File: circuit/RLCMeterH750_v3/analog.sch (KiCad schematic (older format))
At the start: 100 parts, among them J4 DUT, U10 AD8031, U11 AD8031, U12 AD9833, U13 AD8221, U14 AD8221, U16 AD8031, U17 AD8031, U19 FSA3357L8X, U20 FSA3357L8X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

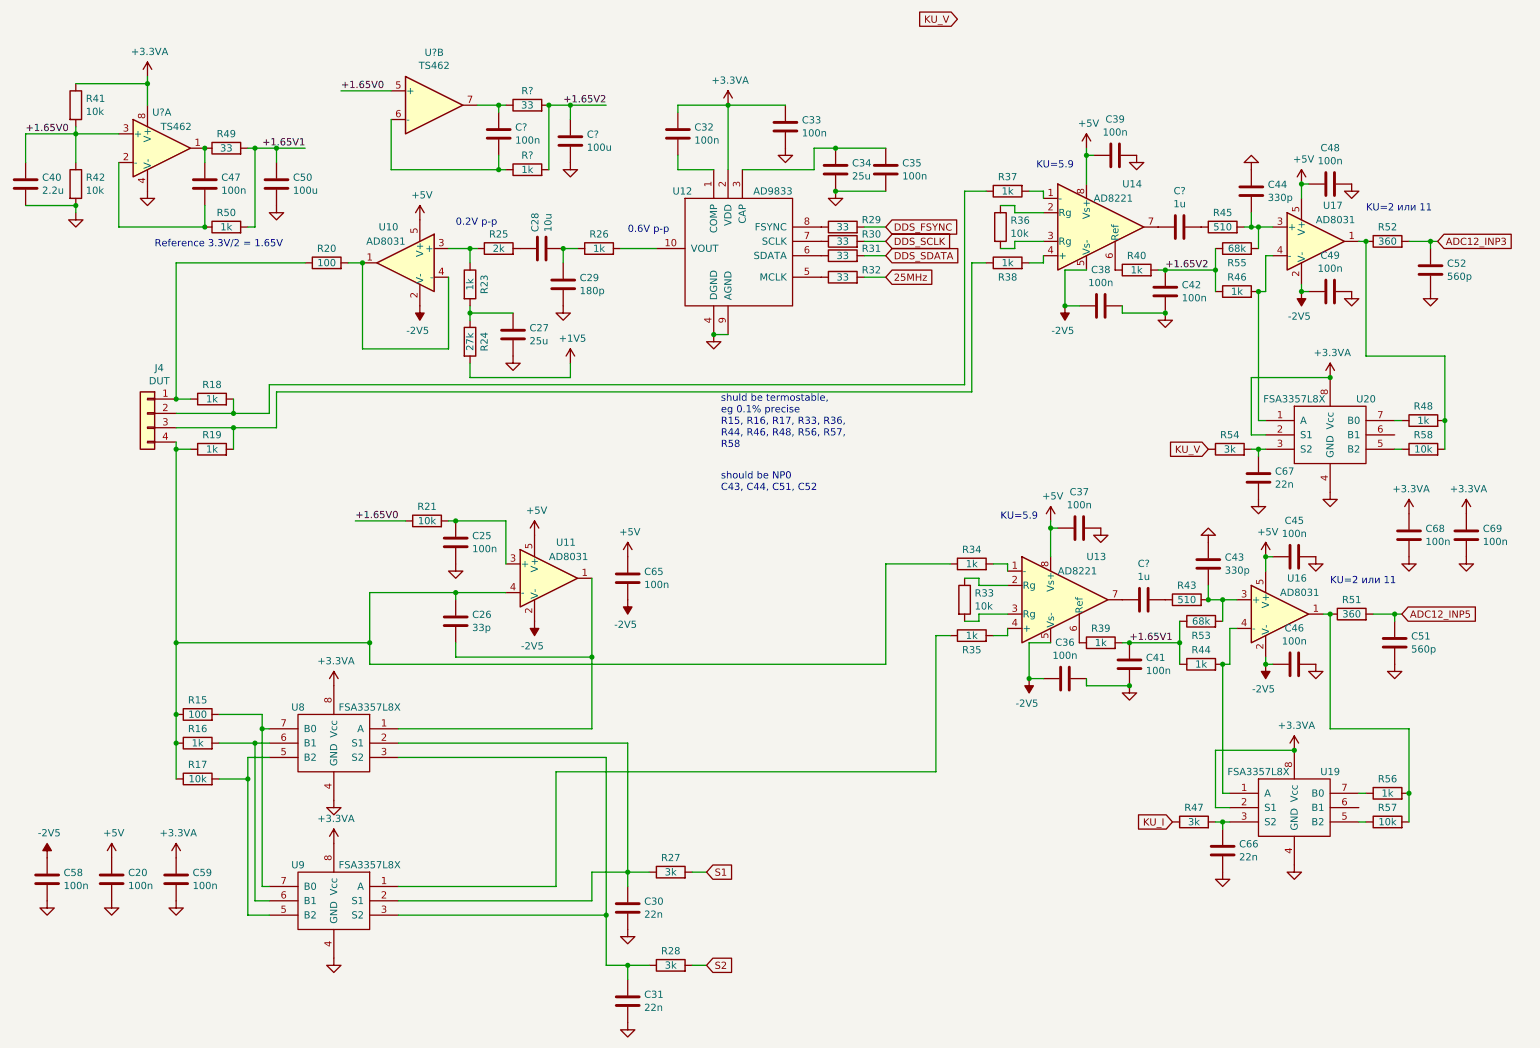
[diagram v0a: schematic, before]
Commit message: - gain_V gain_I надо было умножать, а не делить.
Раньше не проявлялось, так как коэффициэнты были одинаковыми.
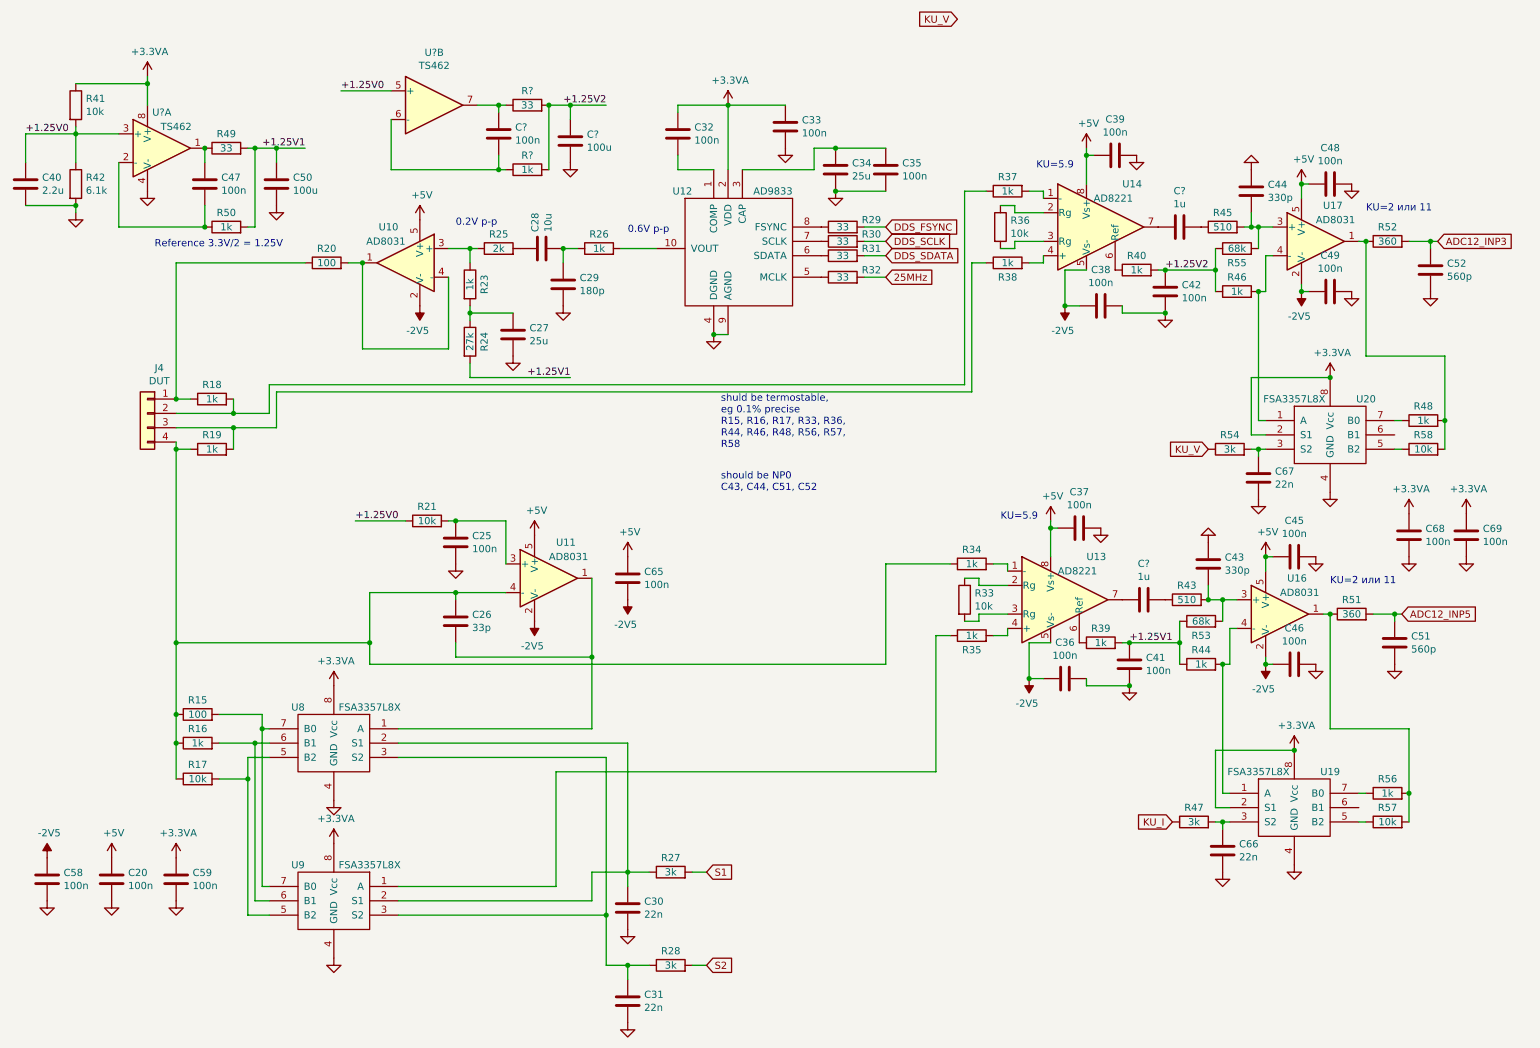
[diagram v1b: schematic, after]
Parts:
- R42: value 10k -> 6.1k
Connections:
- net +1V5 is gone; now on net +1.25V1: R24.2
- net +1.65V0 renamed +1.25V0
- net +1.65V1 renamed +1.25V1
- net +1.65V2 renamed +1.25V2
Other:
- note added: "Reference 3.3V/2 = 1.25V"
- note removed: "Reference 3.3V/2 = 1.65V"
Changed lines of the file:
@@
 Connection ~ 2300 1250
 Text Notes 1600 1950 0    50   ~ 0
-Reference 3.3V/2 = 1.65V
+Reference 3.3V/2 = 1.25V
 $Comp
 L Device:R R42
@@
 P 1050 1500
 F 0 "R42" H 1120 1546 50  0000 L CNN
-F 1 "10k" H 1120 1455 50  0000 L CNN
+F 1 "6.1k" H 1120 1455 50  0000 L CNN
 F 2 "Resistor_SMD:R_0603_1608Metric" V 980 1500 50  0001 C CNN
 F 3 "~" H 1050 1500 50  0001 C CNN
@@
 	1    0    0    -1
 $EndComp
-$Comp
-L power:+1V5 #PWR0181
-U 1 1 5DBA7330
-P 4500 2750
-F 0 "#PWR0181" H 4500 2600 50  0001 C CNN
-F 1 "+1V5" H 4515 2923 50  0000 C CNN
-F 2 "" H 4500 2750 50  0001 C CNN
-F 3 "" H 4500 2750 50  0001 C CNN
-	1    4500 2750
-	1    0    0    -1
-$EndComp
 Wire Wire Line
 	3800 2750 3800 2850
 Wire Wire Line
 	3800 2850 4500 2850
-Wire Wire Line
-	4500 2850 4500 2750
 $Comp
 L Amplifier_Operational:MCP6001-OT U11
@@
 $EndComp
 Text Label 700  1150 0    50   ~ 0
-+1.65V0
++1.25V0
 Wire Wire Line
 	3000 3850 3350 3850
-Text Label 3000 3850 0    50   ~ 0
-+1.65V0
 $Comp
 L Amplifier_Operational:NE5532 U?
@@
 	3250 850  2900 850
 Text Label 2900 850  0    50   ~ 0
-+1.65V0
++1.25V0
 Wire Wire Line
 	2300 1250 2450 1250
@@
 Connection ~ 2450 1250
 Text Label 2350 1250 0    50   ~ 0
-+1.65V1
++1.25V1
 Text Label 4450 950  0    50   ~ 0
-+1.65V2
++1.25V2
 Connection ~ 4350 950
 $Comp
@@
 	4500 950  4750 950
 Text Label 8650 2100 0    50   ~ 0
-+1.65V2
++1.25V2
 Text Label 8400 4700 0    50   ~ 0
-+1.65V1
++1.25V1
 $Comp
 L Device:C C?
@@
 Text Notes 5550 3650 0    50   ~ 0
 should be NP0\nC43, C44, C51, C52
+Text Label 3000 3850 0    50   ~ 0
++1.25V0
+Text Label 4200 2850 0    50   ~ 0
++1.25V1
 $EndSCHEMATC

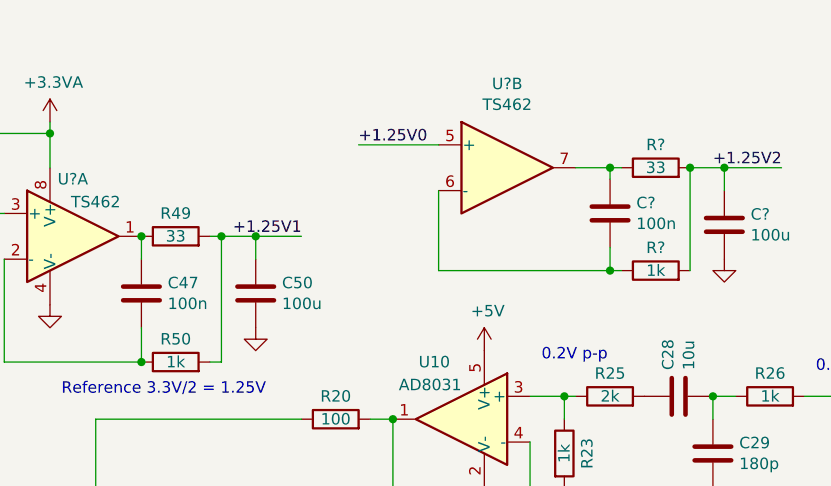
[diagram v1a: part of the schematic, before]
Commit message: - 0 ом резистор на выходе ОУ
- не скалируется график фазы
- стандартные частоты расположены по ряду E12 (экспоненциально)
- добавили коэффииэнты к графикам (KOm, MOm и т.д.)
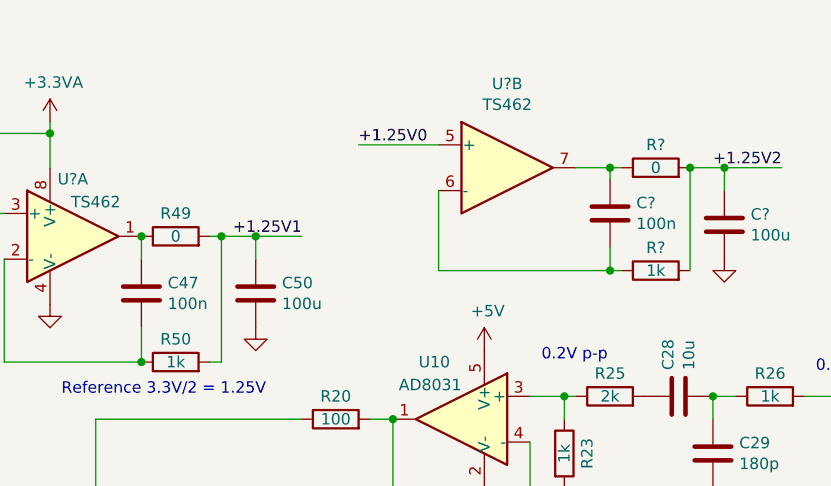
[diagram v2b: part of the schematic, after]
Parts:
- R49, R?: value 33 -> 0
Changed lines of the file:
@@
 P 2100 1250
 F 0 "R49" V 2200 1250 50  0000 C CNN
-F 1 "33" V 2100 1250 50  0000 C CNN
+F 1 "0" V 2100 1250 50  0000 C CNN
 F 2 "Resistor_SMD:R_0603_1608Metric" V 2030 1250 50  0001 C CNN
 F 3 "~" H 2100 1250 50  0001 C CNN
@@
 P 4200 950
 F 0 "R?" V 4300 950 50  0000 C CNN
-F 1 "33" V 4200 950 50  0000 C CNN
+F 1 "0" V 4200 950 50  0000 C CNN
 F 2 "Resistor_SMD:R_0603_1608Metric" V 4130 950 50  0001 C CNN
 F 3 "~" H 4200 950 50  0001 C CNN

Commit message: - все наши страдания с нелинейностью ADC
- debug menu
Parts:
- added C?: 68p, Capacitor_SMD:C_0603_1608Metric, symbol Device:C
- C? (x2): value 1u -> 25u
- R53, R55: value 68k -> 10k
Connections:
- net at C26.1, J4.4 (Pin_4), R15.1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: now also C?.2
- net at R17.2, U8.5 (B2), U9.5 (B2): now also C?.1
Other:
- note added: "Вместо резисторов\nиcпользуем LDO 1.2V"
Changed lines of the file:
@@
 	2400 6600 2250 6600
 Wire Wire Line
-	2250 6600 2250 5650
+	2250 6600 2250 5800
 Wire Wire Line
 	2250 5500 2400 5500
@@
 P 9150 1950
 F 0 "R55" V 9050 1950 50  0000 C CNN
-F 1 "68k" V 9150 1950 50  0000 C CNN
+F 1 "10k" V 9150 1950 50  0000 C CNN
 F 2 "Resistor_SMD:R_0603_1608Metric" V 9080 1950 50  0001 C CNN
 F 3 "~" H 9150 1950 50  0001 C CNN
@@
 P 8900 4550
 F 0 "R53" V 8800 4550 50  0000 C CNN
-F 1 "68k" V 8900 4550 50  0000 C CNN
+F 1 "10k" V 8900 4550 50  0000 C CNN
 F 2 "Resistor_SMD:R_0603_1608Metric" V 8830 4550 50  0001 C CNN
 F 3 "~" H 8900 4550 50  0001 C CNN
@@
 P 8500 4400
 F 0 "C?" V 8248 4400 50  0000 C CNN
-F 1 "1u" V 8339 4400 50  0000 C CNN
+F 1 "25u" V 8339 4400 50  0000 C CNN
 F 2 "Capacitor_SMD:C_0603_1608Metric" H 8538 4250 50  0001 C CNN
 F 3 "~" H 8500 4400 50  0001 C CNN
@@
 P 8750 1800
 F 0 "C?" V 8498 1800 50  0000 C CNN
-F 1 "1u" V 8589 1800 50  0000 C CNN
+F 1 "25u" V 8589 1800 50  0000 C CNN
 F 2 "Capacitor_SMD:C_0603_1608Metric" H 8788 1650 50  0001 C CNN
 F 3 "~" H 8750 1800 50  0001 C CNN
@@
 Text Label 4200 2850 0    50   ~ 0
 +1.25V1
+Text Notes 600  750  0    50   ~ 0
+Вместо резисторов\nиcпользуем LDO 1.2V
+$Comp
+L Device:C C?
+U 1 1 5E38BDC7
+P 2050 5800
+F 0 "C?" H 2165 5846 50  0000 L CNN
+F 1 "68p" H 2165 5755 50  0000 L CNN
+F 2 "Capacitor_SMD:C_0603_1608Metric" H 2088 5650 50  0001 C CNN
+F 3 "~" H 2050 5800 50  0001 C CNN
+	1    2050 5800
+	0    1    1    0
+$EndComp
+Wire Wire Line
+	2200 5800 2250 5800
+Connection ~ 2250 5800
+Wire Wire Line
+	2250 5800 2250 5650
+Wire Wire Line
+	1900 5800 1750 5800
+Wire Wire Line
+	1750 5800 1750 5650
+Connection ~ 1750 5650
 $EndSCHEMATC

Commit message: C47, C? 100n -> 100p, R33, R36 10k -> 15k
C47, C? исправлен номинал на 100 pF
R33, R36 исправлен номинал на 15 КОм
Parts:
- C47, C?: value 100n -> 100p
- R33, R36: value 10k -> 15k
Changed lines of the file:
@@
 P 7500 1800
 F 0 "R36" H 7570 1846 50  0000 L CNN
-F 1 "10k" H 7570 1755 50  0000 L CNN
+F 1 "15k" H 7570 1755 50  0000 L CNN
 F 2 "Resistor_SMD:R_0603_1608Metric" V 7430 1800 50  0001 C CNN
 F 3 "~" H 7500 1800 50  0001 C CNN
@@
 P 1950 1500
 F 0 "C47" H 2065 1546 50  0000 L CNN
-F 1 "100n" H 2065 1455 50  0000 L CNN
+F 1 "100p" H 2065 1455 50  0000 L CNN
 F 2 "Capacitor_SMD:C_0603_1608Metric" H 1988 1350 50  0001 C CNN
 F 3 "~" H 1950 1500 50  0001 C CNN
@@
 P 7250 4400
 F 0 "R33" H 7320 4446 50  0000 L CNN
-F 1 "10k" H 7320 4355 50  0000 L CNN
+F 1 "15k" H 7320 4355 50  0000 L CNN
 F 2 "Resistor_SMD:R_0603_1608Metric" V 7180 4400 50  0001 C CNN
 F 3 "~" H 7250 4400 50  0001 C CNN
@@
 P 4000 1150
 F 0 "C?" H 4115 1196 50  0000 L CNN
-F 1 "100n" H 4115 1105 50  0000 L CNN
+F 1 "100p" H 4115 1105 50  0000 L CNN
 F 2 "Capacitor_SMD:C_0603_1608Metric" H 4038 1000 50  0001 C CNN
 F 3 "~" H 4000 1150 50  0001 C CNN
